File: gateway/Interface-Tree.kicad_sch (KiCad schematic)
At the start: 0 parts

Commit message: Working on version 1.0.0
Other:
- note added: "I2C1: I2C"
- note added: "UART4: Thread"
- note added: "UART_1: Zigbee"
- note added: "UART_2: wMBus"
- note added: "UART_3: Console"
- note added: "USB1: OTG"
- note added: "USB2: LoRa"
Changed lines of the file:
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@@
 		(company "${COMPANY}")
+	)
+	(text "I2C1: I2C"
+		(exclude_from_sim no)
+		(at 199.898 176.784 0)
+		(effects
+			(font
+				(size 1.27 1.27)
+			)
+		)
+	)
+	(text "UART4: Thread"
+		(exclude_from_sim no)
+		(at 203.2 192.278 0)
+		(effects
+			(font
+				(size 1.27 1.27)
+			)
+		)
+	)
+	(text "UART_1: Zigbee"
+		(exclude_from_sim no)
+		(at 220.98 171.704 0)
+		(effects
+			(font
+				(size 1.27 1.27)
+			)
+		)
+	)
+	(text "USB1: OTG"
+		(exclude_from_sim no)
+		(at 201.168 185.166 0)
+		(effects
+			(font
+				(size 1.27 1.27)
+			)
+		)
+	)
+	(text "UART_3: Console"
+		(exclude_from_sim no)
+		(at 221.742 176.784 0)
+		(effects
+			(font
+				(size 1.27 1.27)
+			)
+		)
+	)
+	(text "UART_2: wMBus"
+		(exclude_from_sim no)
+		(at 221.488 174.498 0)
+		(effects
+			(font
+				(size 1.27 1.27)
+			)
+		)
+	)
+	(text "USB2: LoRa"
+		(exclude_from_sim no)
+		(at 201.422 181.61 0)
+		(effects
+			(font
+				(size 1.27 1.27)
+			)
+		)
 	)
 	(text_box "[${#}] ${TITLE}"

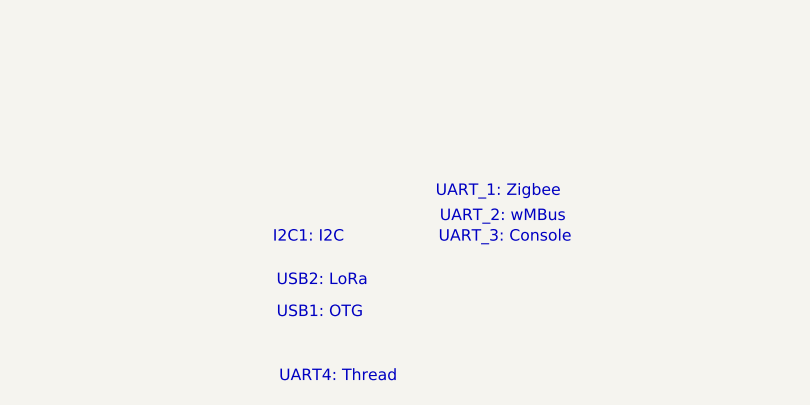
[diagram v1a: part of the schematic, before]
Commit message: Update pin mappings
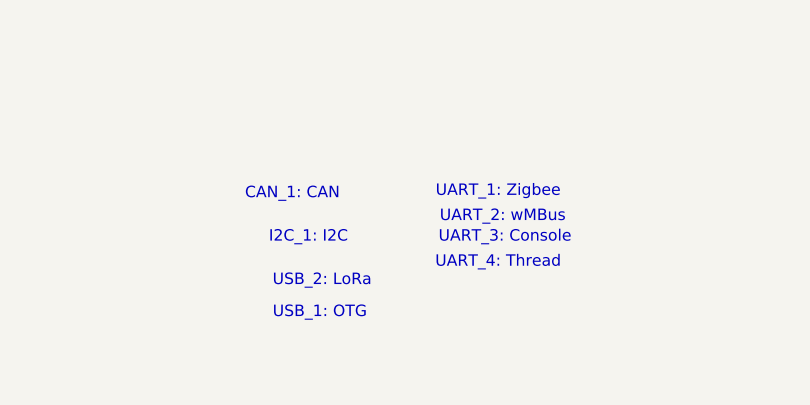
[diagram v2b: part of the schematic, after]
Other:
- note added: "CAN_1: CAN"
- note added: "I2C_1: I2C"
- note added: "UART_4: Thread"
- note added: "USB_1: OTG"
- note added: "USB_2: LoRa"
- note removed: "I2C1: I2C"
- note removed: "UART4: Thread"
- note removed: "USB1: OTG"
- note removed: "USB2: LoRa"
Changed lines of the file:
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@@
 		(company "${COMPANY}")
 	)
-	(text "I2C1: I2C"
+	(text "I2C_1: I2C"
 		(exclude_from_sim no)
 		(at 199.898 176.784 0)
@@
 		)
 	)
-	(text "UART4: Thread"
+	(text "CAN_1: CAN"
 		(exclude_from_sim no)
-		(at 203.2 192.278 0)
+		(at 198.12 171.958 0)
+		(effects
+			(font
+				(size 1.27 1.27)
+			)
+		)
+	)
+	(text "UART_4: Thread"
+		(exclude_from_sim no)
+		(at 220.98 179.578 0)
 		(effects
 			(font
@@
 		)
 	)
-	(text "USB1: OTG"
+	(text "USB_1: OTG"
 		(exclude_from_sim no)
 		(at 201.168 185.166 0)
@@
 		)
 	)
-	(text "USB2: LoRa"
+	(text "USB_2: LoRa"
 		(exclude_from_sim no)
 		(at 201.422 181.61 0)
